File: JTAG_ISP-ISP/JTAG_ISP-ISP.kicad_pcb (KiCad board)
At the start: 2 copper layers, 23.1 x 46.1 mm, 11 parts, among them J1 Conn_02x03_Counter_Clockwise, J2 Conn_01x08, J3 Conn_01x08

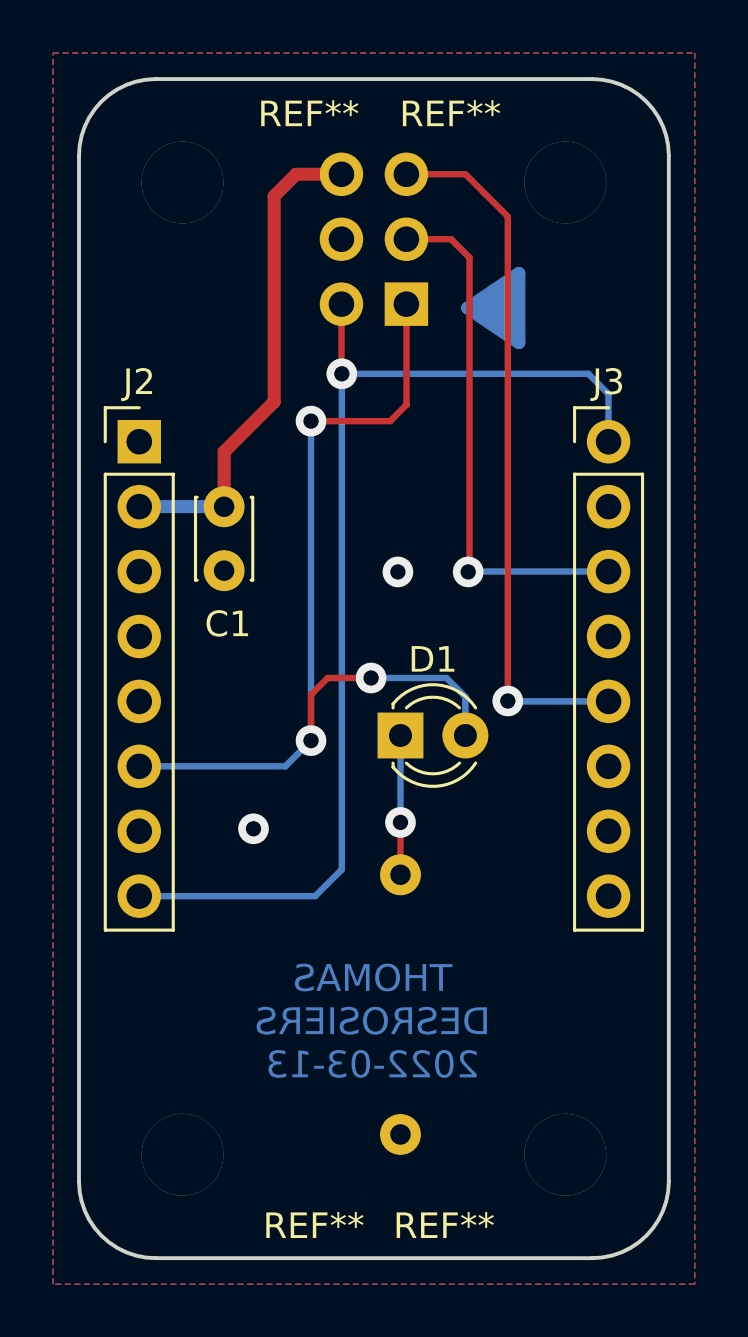
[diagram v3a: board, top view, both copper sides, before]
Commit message: # [PCB] ~ Augmentation de la largeur des traces et du dégagement des traces à 20 mils.
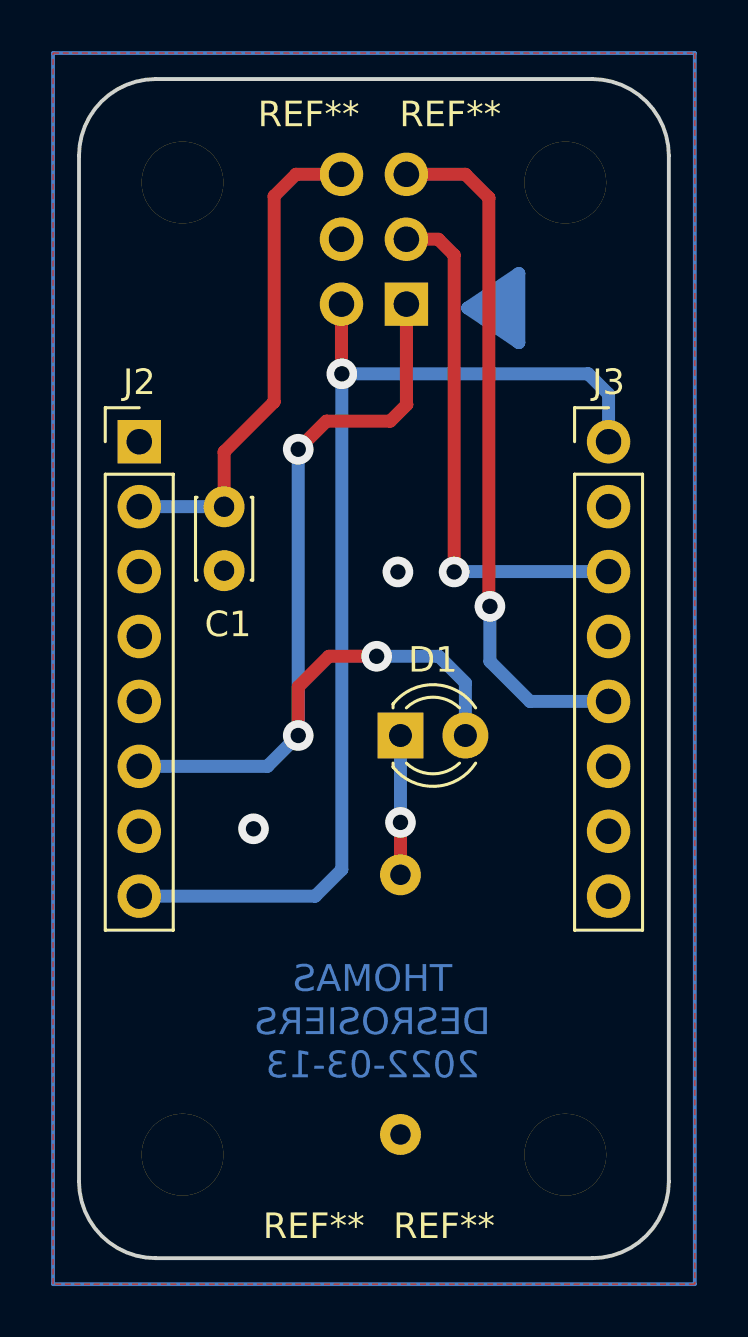
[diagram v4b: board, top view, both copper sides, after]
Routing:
- net MISO: track 37.7 -> 38.5 mm
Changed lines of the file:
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@@
     (pad_to_mask_clearance 0)
     (aux_axis_origin 143.806012 60.297568)
+    (grid_origin 143.806012 60.297568)
     (pcbplotparams
       (layerselection 0x0001000_ffffffff)
@@
   )
   (footprint "Resistor_THT:R_Axial_DIN0207_L6.3mm_D2.5mm_P10.16mm_Horizontal" (layer "B.Cu")
-    (at 157.4 92.45 -90)
+    (at 157.39999 92.450006 -90)
     (descr "Resistor, Axial_DIN0207 series, Axial, Horizontal, pin pitch=10.16mm, 0.25W = 1/4W, length*diameter=6.3*2.5mm^2, http://cdn-reichelt.de/documents/datenblatt/B400/1_4W%23YAG.pdf")
     (tags "Resistor Axial_DIN0207 series Axial Horizontal pin pitch 10.16mm 0.25W = 1/4W length 6.3mm diameter 2.5mm")
@@
     )
   )
+  (gr_rect (start 143.806012 60.297568) (end 168.915994 108.466001) (layer "B.Cu") (width 0.15) (fill none))
   (gr_arc (start 167.9 104.45) (mid 167.02132 106.57132) (end 164.9 107.45) (layer "Edge.Cuts") (width 0.15))
   (gr_arc (start 164.9 61.31548) (mid 167.02132 62.19416) (end 167.9 64.31548) (layer "Edge.Cuts") (width 0.15))
@@
   (gr_arc (start 147.822002 107.45) (mid 145.700682 106.57132) (end 144.822002 104.45) (layer "Edge.Cuts") (width 0.15))
   (gr_rect (start 167.899994 61.315473) (end 144.822012 107.450001) (layer "User.1") (width 1.016) (fill none))
-  (gr_rect (start 143.806012 60.297568) (end 168.915994 108.466001) (layer "User.2") (width 0.15) (fill none))
   (gr_rect (start 167.9 61.31548) (end 144.822002 107.45) (layer "User.9") (width 0.15) (fill none))
   (gr_text "THOMAS\nDESROSIERS\n2022-03-13" (at 156.306012 98.197568) (layer "B.Cu")
@@
   (via (at 151.65 90.65) (size 1.2) (drill 0.6) (layers "F.Cu" "B.Cu") (free) (net 2))
   (via (at 157.3 80.6) (size 1.2) (drill 0.6) (layers "F.Cu" "B.Cu") (free) (net 2))
-  (segment (start 157.65 74.05) (end 157.631003 74.031003) (width 0.25) (layer "F.Cu") (net 3))
-  (segment (start 154.55 84.75) (end 153.9 85.4) (width 0.25) (layer "F.Cu") (net 3))
-  (segment (start 153.9 74.7) (end 157 74.7) (width 0.25) (layer "F.Cu") (net 3))
-  (segment (start 156.25 84.75) (end 154.55 84.75) (width 0.25) (layer "F.Cu") (net 3))
-  (segment (start 153.9 85.4) (end 153.9 87.2) (width 0.25) (layer "F.Cu") (net 3))
-  (segment (start 157.631003 74.031003) (end 157.631003 70.122567) (width 0.25) (layer "F.Cu") (net 3))
-  (segment (start 157 74.7) (end 157.65 74.05) (width 0.25) (layer "F.Cu") (net 3))
-  (via (at 156.25 84.75) (size 1.2) (drill 0.6) (layers "F.Cu" "B.Cu") (net 3))
-  (via (at 153.9 74.7) (size 1.2) (drill 0.6) (layers "F.Cu" "B.Cu") (net 3))
-  (via (at 153.9 87.2) (size 1.2) (drill 0.6) (layers "F.Cu" "B.Cu") (net 3))
-  (segment (start 159.2 84.75) (end 156.25 84.75) (width 0.25) (layer "B.Cu") (net 3))
-  (segment (start 152.894233 88.205767) (end 153.9 87.2) (width 0.25) (layer "B.Cu") (net 3))
-  (segment (start 153.9 87.2) (end 153.9 74.7) (width 0.25) (layer "B.Cu") (net 3))
-  (segment (start 159.94 85.49) (end 159.2 84.75) (width 0.25) (layer "B.Cu") (net 3))
-  (segment (start 159.94 87.2) (end 159.94 85.49) (width 0.25) (layer "B.Cu") (net 3))
-  (segment (start 147.179995 88.205767) (end 152.894233 88.205767) (width 0.25) (layer "B.Cu") (net 3))
+  (segment (start 157.65 74.05) (end 157.631003 74.031003) (width 0.508) (layer "F.Cu") (net 3))
+  (segment (start 153.4 85.1) (end 153.4 87) (width 0.508) (layer "F.Cu") (net 3))
+  (segment (start 157.631003 74.031003) (end 157.631003 70.122567) (width 0.508) (layer "F.Cu") (net 3))
+  (segment (start 153.4 75.8) (end 154.5 74.7) (width 0.508) (layer "F.Cu") (net 3))
+  (segment (start 156.467512 83.9) (end 154.6 83.9) (width 0.508) (layer "F.Cu") (net 3))
+  (segment (start 154.6 83.9) (end 153.4 85.1) (width 0.508) (layer "F.Cu") (net 3))
+  (segment (start 157 74.7) (end 157.65 74.05) (width 0.508) (layer "F.Cu") (net 3))
+  (segment (start 154.5 74.7) (end 157 74.7) (width 0.508) (layer "F.Cu") (net 3))
+  (via (at 156.467512 83.9) (size 1.2) (drill 0.6) (layers "F.Cu" "B.Cu") (net 3))
+  (via (at 153.4 75.8) (size 1.2) (drill 0.6) (layers "F.Cu" "B.Cu") (net 3))
+  (via (at 153.4 87) (size 1.2) (drill 0.6) (layers "F.Cu" "B.Cu") (net 3))
+  (segment (start 159.94 84.94) (end 159.94 87.2) (width 0.508) (layer "B.Cu") (net 3))
+  (segment (start 152.194233 88.205767) (end 147.179995 88.205767) (width 0.508) (layer "B.Cu") (net 3))
+  (segment (start 153.4 87) (end 152.194233 88.205767) (width 0.508) (layer "B.Cu") (net 3))
+  (segment (start 153.4 87) (end 153.4 75.8) (width 0.508) (layer "B.Cu") (net 3))
+  (segment (start 156.467512 83.9) (end 158.9 83.9) (width 0.508) (layer "B.Cu") (net 3))
+  (segment (start 158.9 83.9) (end 159.94 84.94) (width 0.508) (layer "B.Cu") (net 3))
   (segment (start 155.091003 72.832559) (end 155.106012 72.847568) (width 0.25) (layer "F.Cu") (net 4))
-  (segment (start 155.091003 70.122567) (end 155.091003 72.832559) (width 0.25) (layer "F.Cu") (net 4))
+  (segment (start 155.091003 70.122567) (end 155.091003 72.83257) (width 0.508) (layer "F.Cu") (net 4))
   (via (at 155.106012 72.847568) (size 1.2) (drill 0.6) (layers "F.Cu" "B.Cu") (net 4))
-  (segment (start 165.542011 73.642011) (end 165.542011 75.505767) (width 0.25) (layer "B.Cu") (net 4))
-  (segment (start 147.179995 93.285767) (end 154.064233 93.285767) (width 0.25) (layer "B.Cu") (net 4))
-  (segment (start 155.106012 72.847568) (end 164.747568 72.847568) (width 0.25) (layer "B.Cu") (net 4))
-  (segment (start 154.064233 93.285767) (end 155.106012 92.243988) (width 0.25) (layer "B.Cu") (net 4))
-  (segment (start 164.747568 72.847568) (end 165.542011 73.642011) (width 0.25) (layer "B.Cu") (net 4))
-  (segment (start 155.106012 92.243988) (end 155.106012 72.847568) (width 0.25) (layer "B.Cu") (net 4))
-  (segment (start 160.1 80.55) (end 160.1 68.3) (width 0.25) (layer "F.Cu") (net 5))
-  (segment (start 160.05 80.6) (end 160.1 80.55) (width 0.25) (layer "F.Cu") (net 5))
-  (segment (start 160.1 68.3) (end 159.382567 67.582567) (width 0.25) (layer "F.Cu") (net 5))
-  (segment (start 159.382567 67.582567) (end 157.631003 67.582567) (width 0.25) (layer "F.Cu") (net 5))
-  (via (at 160.05 80.6) (size 1.2) (drill 0.6) (layers "F.Cu" "B.Cu") (net 5))
-  (segment (start 160.064233 80.585767) (end 165.542011 80.585767) (width 0.25) (layer "B.Cu") (net 5))
-  (segment (start 160.05 80.6) (end 160.064233 80.585767) (width 0.25) (layer "B.Cu") (net 5))
-  (segment (start 160.65 65.75) (end 161.6 66.7) (width 0.25) (layer "F.Cu") (net 6))
-  (segment (start 159.942567 65.042567) (end 160.65 65.75) (width 0.25) (layer "F.Cu") (net 6))
-  (segment (start 161.6 66.7) (end 161.6 85.65) (width 0.25) (layer "F.Cu") (net 6))
-  (segment (start 157.631003 65.042567) (end 159.942567 65.042567) (width 0.25) (layer "F.Cu") (net 6))
-  (via (at 161.6 85.65) (size 1.2) (drill 0.6) (layers "F.Cu" "B.Cu") (net 6))
-  (segment (start 161.6 85.65) (end 161.615767 85.665767) (width 0.25) (layer "B.Cu") (net 6))
-  (segment (start 161.615767 85.665767) (end 165.542011 85.665767) (width 0.25) (layer "B.Cu") (net 6))
-  (segment (start 157.39999 92.450006) (end 157.39999 90.399997) (width 0.25) (layer "F.Cu") (net 16))
+  (segment (start 165.542011 73.642011) (end 165.542011 75.505767) (width 0.508) (layer "B.Cu") (net 4))
+  (segment (start 147.179995 93.285767) (end 154.064233 93.285767) (width 0.508) (layer "B.Cu") (net 4))
+  (segment (start 155.106012 72.847568) (end 164.747568 72.847568) (width 0.508) (layer "B.Cu") (net 4))
+  (segment (start 154.064233 93.285767) (end 155.106012 92.243988) (width 0.508) (layer "B.Cu") (net 4))
+  (segment (start 164.747568 72.847568) (end 165.542011 73.642011) (width 0.508) (layer "B.Cu") (net 4))
+  (segment (start 155.106012 92.243988) (end 155.106012 72.847568) (width 0.508) (layer "B.Cu") (net 4))
+  (segment (start 159.5 68.2) (end 158.882567 67.582567) (width 0.508) (layer "F.Cu") (net 5))
+  (segment (start 158.882567 67.582567) (end 157.631003 67.582567) (width 0.508) (layer "F.Cu") (net 5))
+  (segment (start 159.5 80.6) (end 159.5 68.2) (width 0.508) (layer "F.Cu") (net 5))
+  (via (at 159.5 80.6) (size 1.2) (drill 0.6) (layers "F.Cu" "B.Cu") (net 5))
+  (segment (start 159.514233 80.585767) (end 165.542011 80.585767) (width 0.508) (layer "B.Cu") (net 5))
+  (segment (start 159.5 80.6) (end 159.514233 80.585767) (width 0.508) (layer "B.Cu") (net 5))
+  (segment (start 160.861511 81.908778) (end 160.861511 65.961511) (width 0.508) (layer "F.Cu") (net 6))
+  (segment (start 160.9 81.947267) (end 160.861511 81.908778) (width 0.508) (layer "F.Cu") (net 6))
+  (segment (start 159.942567 65.042567) (end 157.631003 65.042567) (width 0.508) (layer "F.Cu") (net 6))
+  (segment (start 160.861511 65.961511) (end 159.942567 65.042567) (width 0.508) (layer "F.Cu") (net 6))
+  (via (at 160.9 81.947267) (size 1.2) (drill 0.6) (layers "F.Cu" "B.Cu") (net 6))
+  (segment (start 162.465767 85.665767) (end 165.542011 85.665767) (width 0.508) (layer "B.Cu") (net 6))
+  (segment (start 160.9 84.1) (end 162.465767 85.665767) (width 0.508) (layer "B.Cu") (net 6))
+  (segment (start 160.9 81.947267) (end 160.9 84.1) (width 0.508) (layer "B.Cu") (net 6))
+  (segment (start 157.39999 92.450006) (end 157.39999 90.399997) (width 0.508) (layer "F.Cu") (net 16))
   (via (at 157.4 90.4) (size 1.2) (drill 0.6) (layers "F.Cu" "B.Cu") (net 16))
-  (segment (start 157.4 87.2) (end 157.4 90.4) (width 0.25) (layer "B.Cu") (net 16))
+  (segment (start 157.4 87.2) (end 157.4 90.4) (width 0.508) (layer "B.Cu") (net 16))
   (zone (net 2) (net_name "GND") (layers F&B.Cu) (hatch edge 0.508)
     (connect_pads (clearance 0.508))

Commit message: # [PCB] + Ajout d'un trou au bas du PCB pour le projet du projet HDR pour laisser passer la sur le PCB d'en dessous. - Suppression du texte (nom & date) sur le PCB du bas puisqu'il ne sera pas le plus visible.
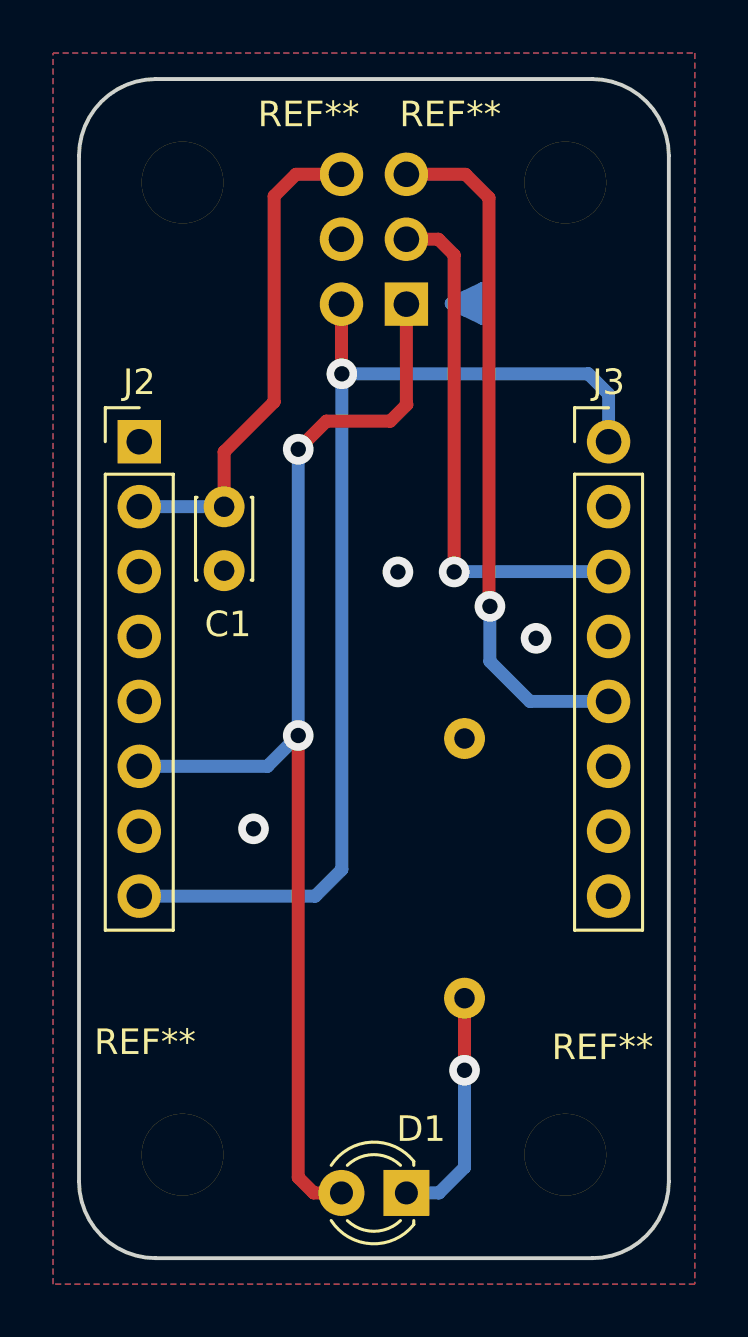
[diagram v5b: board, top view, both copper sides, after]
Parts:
- removed the REF** at (161.3, 70.6)
- added REF**: Fleche_small, THOMAS_library:Fleche_small, B.Cu at (160.6, 70.5)
- moved D1 17.9 mm to (157.6, 104.9), turned to 180 degrees
- moved R1 5.44 mm to (159.9, 97.3), turned to 90 degrees
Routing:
- net MISO: track 38.5 -> 46.1 mm, vias 3 -> 2
- net Net-(D1-Pad1): track 5.25 -> 9.31 mm
- net GND: vias 2 -> 3
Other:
- board text removed: "THOMAS DESROSIERS 2022-03-13"

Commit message: # [PCB] + Ajout d'un trou dans le haut du PCB du projet HDR pour pouvoir y fixer une dragone. ~ Modification de l'empreinte du JTAG. - Non affichage des référence pour les trous et les flèches sur le PCB des 2 projets.
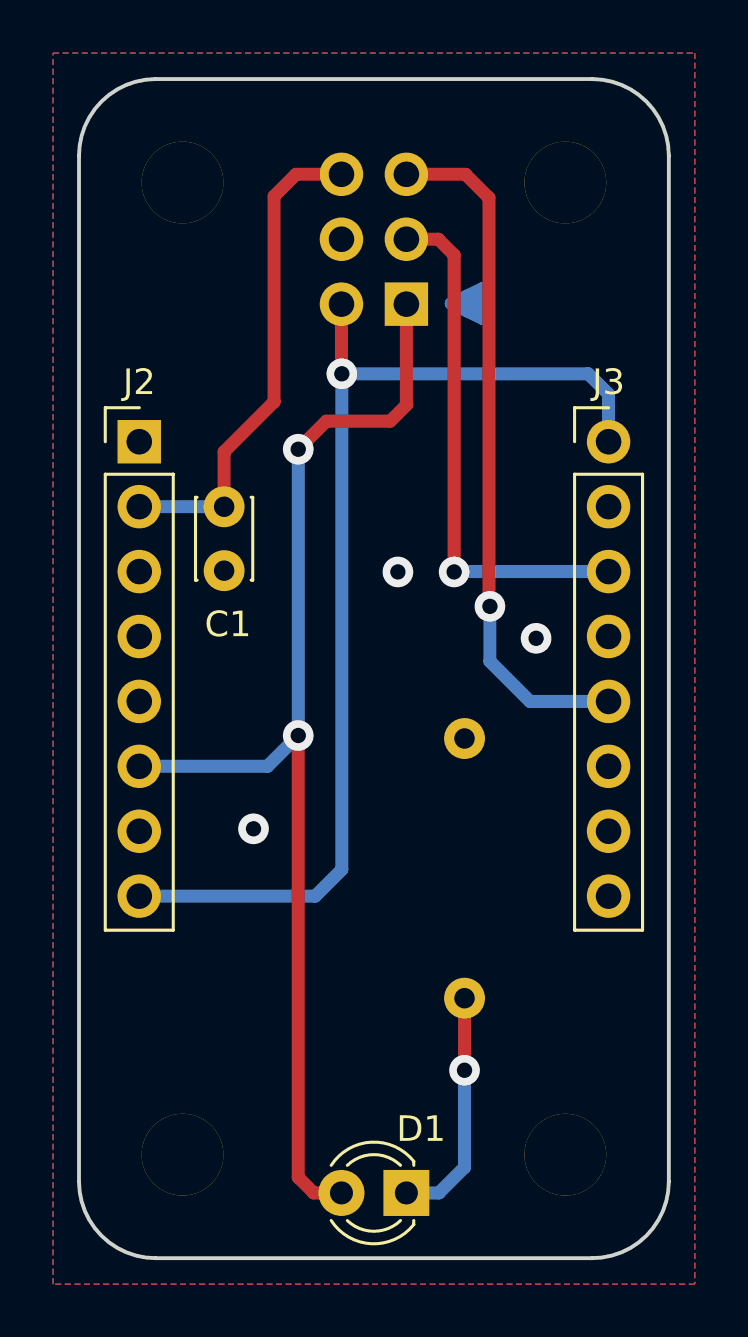
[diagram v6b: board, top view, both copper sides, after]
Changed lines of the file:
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@@
     (tags "mounting hole 3.2mm no annular m3")
     (attr exclude_from_pos_files exclude_from_bom)
-    (fp_text reference "REF**" (at 1.456022 -4.202428) (layer "F.SilkS")
+    (fp_text reference "REF**" (at 1.456022 -4.202428) (layer "F.SilkS") hide
       (effects (font (size 1 1) (thickness 0.15)))
     )
@@
       (effects (font (size 1 1) (thickness 0.15)))
     )
-    (fp_text user "${REFERENCE}" (at 1.456022 -4.202428) (layer "F.Fab")
+    (fp_text user "${REFERENCE}" (at 1.456022 -4.202428) (layer "F.Fab") hide
       (effects (font (size 1 1) (thickness 0.15)))
     )
@@
     (tags "mounting hole 3.2mm no annular m3")
     (attr exclude_from_pos_files exclude_from_bom)
-    (fp_text reference "REF**" (at -4.500012 -2.665988) (layer "F.SilkS")
+    (fp_text reference "REF**" (at -4.500012 -2.665988) (layer "F.SilkS") hide
       (effects (font (size 1 1) (thickness 0.15)))
     )
@@
       (effects (font (size 1 1) (thickness 0.15)))
     )
-    (fp_text user "${REFERENCE}" (at -4.500012 -2.665988) (layer "F.Fab")
+    (fp_text user "${REFERENCE}" (at -4.500012 -2.665988) (layer "F.Fab") hide
       (effects (font (size 1 1) (thickness 0.15)))
     )
@@
     (tags "mounting hole 3.2mm no annular m3")
     (attr exclude_from_pos_files exclude_from_bom)
-    (fp_text reference "REF**" (at -1.465979 -4.402428) (layer "F.SilkS")
+    (fp_text reference "REF**" (at -1.465979 -4.402428) (layer "F.SilkS") hide
       (effects (font (size 1 1) (thickness 0.15)))
     )
@@
       (effects (font (size 1 1) (thickness 0.15)))
     )
-    (fp_text user "${REFERENCE}" (at -1.465979 -4.402428) (layer "F.Fab")
+    (fp_text user "${REFERENCE}" (at -1.465979 -4.402428) (layer "F.Fab") hide
       (effects (font (size 1 1) (thickness 0.15)))
     )
@@
     (tags "mounting hole 3.2mm no annular m3")
     (attr exclude_from_pos_files exclude_from_bom)
-    (fp_text reference "REF**" (at 4.93401 -2.665988) (layer "F.SilkS")
+    (fp_text reference "REF**" (at 4.93401 -2.665988) (layer "F.SilkS") hide
       (effects (font (size 1 1) (thickness 0.15)))
     )
@@
       (effects (font (size 1 1) (thickness 0.15)))
     )
-    (fp_text user "${REFERENCE}" (at 4.93401 -2.665988) (layer "F.Fab")
+    (fp_text user "${REFERENCE}" (at 4.93401 -2.665988) (layer "F.Fab") hide
       (effects (font (size 1 1) (thickness 0.15)))
     )
@@
   )
   (footprint "THOMAS_library:Fleche_small" (layer "B.Cu")
-    (at 160.612017 70.452568)
-    (fp_text reference "REF**" (at 0.02 1.9 180 unlocked) (layer "B.SilkS")
-      (effects (font (size 1 1) (thickness 0.15)) (justify mirror))
-    )
-    (fp_text value "Fleche_small" (at -0.01 -2.77 180 unlocked) (layer "B.Fab")
-      (effects (font (size 1 1) (thickness 0.15)) (justify mirror))
-    )
-    (fp_text user "${REFERENCE}" (at 0.01 1.89 180 unlocked) (layer "B.Fab")
-      (effects (font (size 1 1) (thickness 0.15)) (justify mirror))
-    )
+    (at 160.612023 70.452564)
+    (fp_text reference "REF**" (at 0.02 1.9 180 unlocked) (layer "B.SilkS") hide
+      (effects (font (size 1 1) (thickness 0.15)) (justify mirror))
+    )
+    (fp_text value "Fleche_small" (at -0.01 -2.77 180 unlocked) (layer "B.Fab") hide
+      (effects (font (size 1 1) (thickness 0.15)) (justify mirror))
+    )
+    (fp_text user "${REFERENCE}" (at 0.01 1.89 180 unlocked) (layer "B.Fab") hide
+      (effects (font (size 1 1) (thickness 0.15)) (justify mirror))
+    )
